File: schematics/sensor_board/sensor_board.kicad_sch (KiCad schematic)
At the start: 6 parts, among them Y1 Crystal

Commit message: I think it is finished.
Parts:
- added C4, C5, C6: 100n, Capacitor_SMD:C_0603_1608Metric_Pad1.08x0.95mm_HandSolder, symbol Device:C
- added J1: Conn_01x06_Pin, Connector_PinHeader_1.27mm:PinHeader_1x06_P1.27mm_Vertical, symbol Connector:Conn_01x06_Pin
- added J2: Conn_01x05_Pin, Connector_PinHeader_1.27mm:PinHeader_1x05_P1.27mm_Vertical, symbol Connector:Conn_01x05_Pin
- added R2, R3, R4, R5, R6, R7, R8, R9: 10k, Resistor_SMD:R_0603_1608Metric_Pad0.98x0.95mm_HandSolder, symbol Device:R
- C1, C2, C3: footprint (none) -> Capacitor_SMD:C_0603_1608Metric_Pad1.08x0.95mm_HandSolder
- R1: value R -> 10k; footprint (none) -> Resistor_SMD:R_0603_1608Metric_Pad0.98x0.95mm_HandSolder
- U1: footprint (none) -> Package_LGA:LGA-28_5.2x3.8mm_P0.5mm
- Y1: footprint (none) -> Crystal:Crystal_HC52-8mm_Vertical
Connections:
- net GND: now also U1.5 (PS1), U1.6 (PS0/WAKE), C4.2, C5.2, C6.2, J1.2 (Pin_2), J2.2 (Pin_2), R3.2
- net VDD: now also C5.1, C6.1, J1.1 (Pin_1), J2.1 (Pin_1), R2.1, R4.1, R5.1, R6.1, R7.1, R8.1, R9.1
- net intn: now reaches U1.14 (H_INTN)
- net intn: now also J1.5 (Pin_5)
- net at U1.15 (ENV_SCL): now also R5.2
- net at U1.16 (ENV_SDA): now also R4.2
- net i2c_addr_sel: now reaches U1.17 (SA0/H_MOSI)
- net i2c_addr_sel: now also R2.2, R3.1
- net at U1.18 (H_CSN): now also R7.2
- net scl: now reaches U1.19 (H_SCL/SCK/RX)
- net scl: now also J1.4 (Pin_4), J2.4 (Pin_4), R8.2
- net sda: now reaches U1.20 (H_SDA/H_MISO/TX)
- net sda: now also J1.3 (Pin_3), J2.3 (Pin_3), R9.2
- net at U1.4 (BOOTN): now also R6.2
- net at U1.9 (CAP): now also C4.1
- new net intn_next: J1.6 (Pin_6), J2.5 (Pin_5)
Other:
- note added: "Add one of these two for I2C address selection."
- note added: "Sampled on reset. If low, enters bootloader mode."
- note added: "This might be not needed. In ref. design it is left not connected."

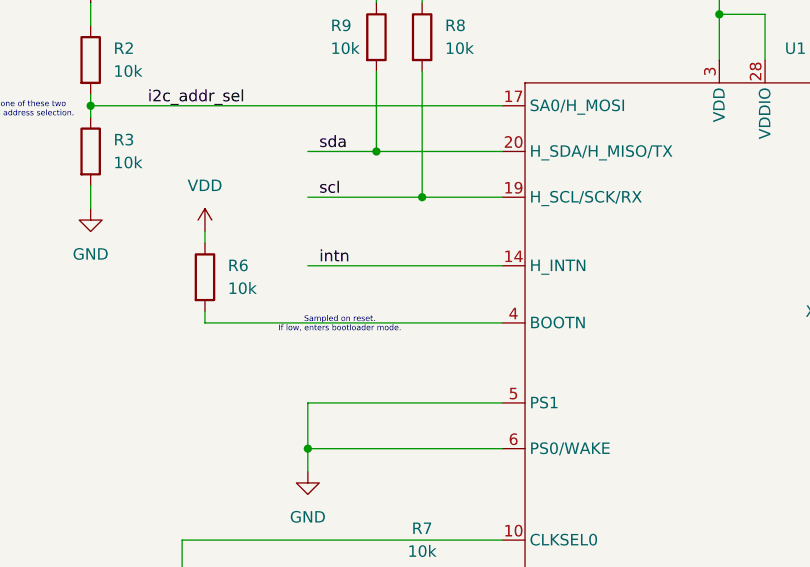
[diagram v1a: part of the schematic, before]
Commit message: Added resistor to the interrupt signal.
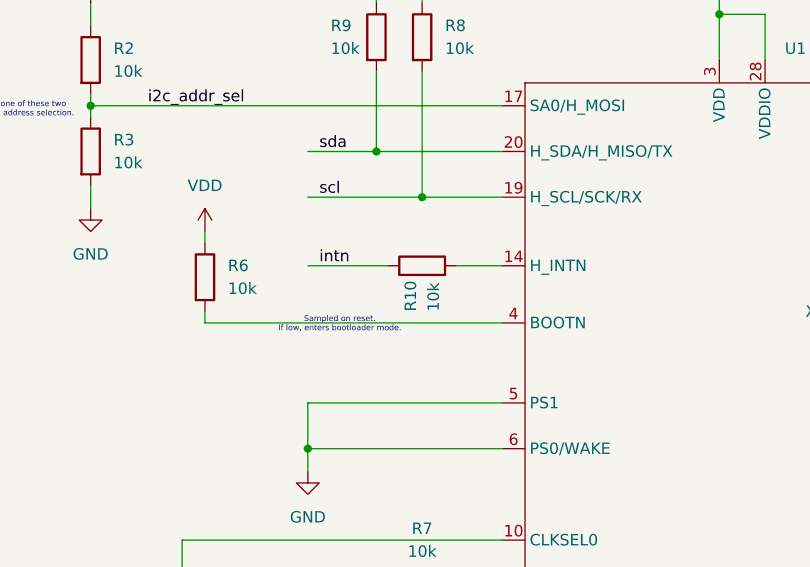
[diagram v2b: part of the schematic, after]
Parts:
- added R10: 10k, Resistor_SMD:R_0603_1608Metric_Pad0.98x0.95mm_HandSolder, symbol Device:R
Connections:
- net intn: now also R10.1; no longer U1.14 (H_INTN)
- new net: R10.2, U1.14 (H_INTN)
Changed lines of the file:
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@@
+	(wire
+		(pts
+			(xy 193.04 105.41) (xy 198.12 105.41)
+		)
+		(stroke
+			(width 0)
+			(type default)
+		)
+	)
 	(wire
 		(pts
@@
 	(wire
 		(pts
-			(xy 176.53 105.41) (xy 198.12 105.41)
-		)
-		(stroke
-			(width 0)
-			(type default)
-		)
-	)
-	(wire
-		(pts
 			(xy 251.46 53.34) (xy 251.46 54.61)
 		)
@@
 		(pts
 			(xy 270.51 148.59) (xy 270.51 153.67)
+		)
+		(stroke
+			(width 0)
+			(type default)
+		)
+	)
+	(wire
+		(pts
+			(xy 176.53 105.41) (xy 185.42 105.41)
 		)
 		(stroke
@@
 					(unit 1)
 				)
+			)
+		)
+	)
+	(symbol
+		(lib_id "Device:R")
+		(at 189.23 105.41 90)
+		(unit 1)
+		(exclude_from_sim no)
+		(in_bom yes)
+		(on_board yes)
+		(dnp no)
+		(property "Reference" "R10"
+			(at 187.96 110.49 0)
+			(effects
+				(font
+					(size 1.27 1.27)
+				)
+				(justify left)
+			)
+		)
+		(property "Value" "10k"
+			(at 190.5 110.49 0)
+			(effects
+				(font
+					(size 1.27 1.27)
+				)
+				(justify left)
+			)
+		)
+		(property "Footprint" "Resistor_SMD:R_0603_1608Metric_Pad0.98x0.95mm_HandSolder"
+			(at 189.23 107.188 90)
+			(effects
+				(font
+					(size 1.27 1.27)
+				)
+				(hide yes)
+			)
+		)
+		(property "Datasheet" "~"
+			(at 189.23 105.41 0)
+			(effects
+				(font
+					(size 1.27 1.27)
+				)
+				(hide yes)
+			)
+		)
+		(property "Description" "Resistor"
+			(at 189.23 105.41 0)
+			(effects
+				(font
+					(size 1.27 1.27)
+				)
+				(hide yes)
+			)
+		)
+		(pin "2"
+		)
+		(pin "1"
+		)
+		(instances
+			(project "sensor_board"
+				(path "/0f022720-add9-458b-9410-e96307841923"
+					(reference "R10")
+					(unit 1)
+				)

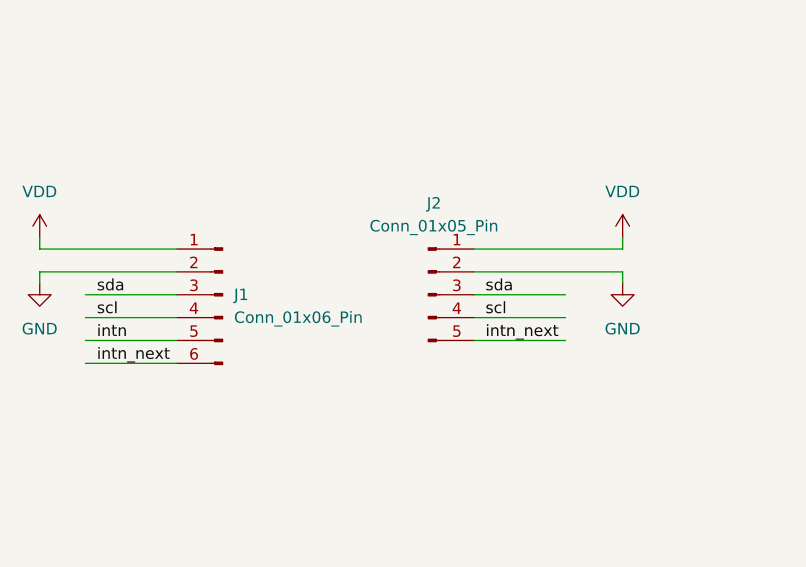
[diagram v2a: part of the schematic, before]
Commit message: Selarated INT, SCL and SDA lines with GND and VDD so that crosstalk is reduced
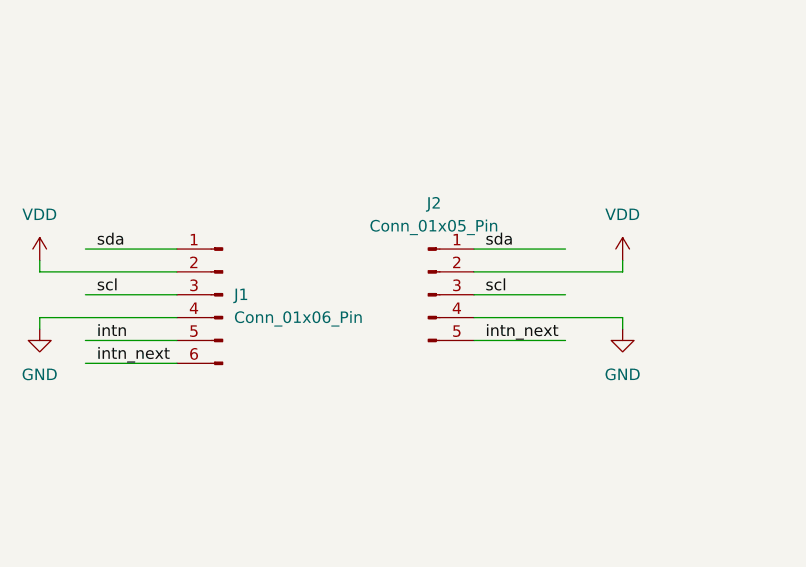
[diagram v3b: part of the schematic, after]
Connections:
- net GND: now also J1.4 (Pin_4), J2.4 (Pin_4); no longer J1.2 (Pin_2), J2.2 (Pin_2)
- net VDD: now also J1.2 (Pin_2), J2.2 (Pin_2); no longer J1.1 (Pin_1), J2.1 (Pin_1)
- net scl: now also J1.3 (Pin_3), J2.3 (Pin_3); no longer J1.4 (Pin_4), J2.4 (Pin_4)
- net sda: now also J1.1 (Pin_1), J2.1 (Pin_1); no longer J1.3 (Pin_3), J2.3 (Pin_3)
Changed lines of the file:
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@@
 	(wire
 		(pts
-			(xy 43.18 100.33) (xy 43.18 101.6)
+			(xy 43.18 102.87) (xy 43.18 104.14)
 		)
 		(stroke
@@
 	(wire
 		(pts
-			(xy 91.44 104.14) (xy 107.95 104.14)
+			(xy 91.44 109.22) (xy 107.95 109.22)
 		)
 		(stroke
@@
 	(wire
 		(pts
-			(xy 48.26 109.22) (xy 58.42 109.22)
+			(xy 48.26 106.68) (xy 58.42 106.68)
 		)
 		(stroke
@@
 	(wire
 		(pts
-			(xy 107.95 100.33) (xy 107.95 101.6)
+			(xy 107.95 102.87) (xy 107.95 104.14)
 		)
 		(stroke
@@
 	(wire
 		(pts
-			(xy 91.44 101.6) (xy 107.95 101.6)
+			(xy 91.44 104.14) (xy 107.95 104.14)
 		)
 		(stroke
@@
 	(wire
 		(pts
-			(xy 43.18 101.6) (xy 58.42 101.6)
+			(xy 43.18 104.14) (xy 58.42 104.14)
 		)
 		(stroke
@@
 	(wire
 		(pts
-			(xy 43.18 104.14) (xy 43.18 105.41)
+			(xy 43.18 109.22) (xy 43.18 110.49)
 		)
 		(stroke
@@
 	(wire
 		(pts
-			(xy 43.18 104.14) (xy 58.42 104.14)
+			(xy 43.18 109.22) (xy 58.42 109.22)
 		)
 		(stroke
@@
 	(wire
 		(pts
-			(xy 107.95 104.14) (xy 107.95 105.41)
+			(xy 107.95 109.22) (xy 107.95 110.49)
 		)
 		(stroke
@@
 	(wire
 		(pts
-			(xy 91.44 106.68) (xy 101.6 106.68)
+			(xy 91.44 101.6) (xy 101.6 101.6)
 		)
 		(stroke
@@
 	(wire
 		(pts
-			(xy 91.44 109.22) (xy 101.6 109.22)
+			(xy 91.44 106.68) (xy 101.6 106.68)
 		)
 		(stroke
@@
 	(wire
 		(pts
-			(xy 48.26 106.68) (xy 58.42 106.68)
+			(xy 48.26 101.6) (xy 58.42 101.6)
 		)
 		(stroke
@@
 	)
 	(label "sda"
-		(at 92.71 106.68 0)
+		(at 92.71 101.6 0)
 		(fields_autoplaced yes)
 		(effects
@@
 	)
 	(label "scl"
-		(at 92.71 109.22 0)
+		(at 92.71 106.68 0)
 		(fields_autoplaced yes)
 		(effects
@@
 	)
 	(label "scl"
-		(at 49.53 109.22 0)
+		(at 49.53 106.68 0)
 		(fields_autoplaced yes)
 		(effects
@@
 	)
 	(label "sda"
-		(at 49.53 106.68 0)
+		(at 49.53 101.6 0)
 		(fields_autoplaced yes)
 		(effects
@@
 	(symbol
 		(lib_id "power:VDD")
-		(at 43.18 100.33 0)
+		(at 43.18 102.87 0)
 		(unit 1)
 		(exclude_from_sim no)
@@
 		(fields_autoplaced yes)
 		(property "Reference" "#PWR019"
-			(at 43.18 104.14 0)
+			(at 43.18 106.68 0)
 			(effects
 				(font
@@
 		)
 		(property "Value" "VDD"
-			(at 43.18 95.25 0)
+			(at 43.18 97.79 0)
 			(effects
 				(font
@@
 		)
 		(property "Footprint" ""
-			(at 43.18 100.33 0)
+			(at 43.18 102.87 0)
 			(effects
 				(font
@@
 		)
 		(property "Datasheet" ""
-			(at 43.18 100.33 0)
+			(at 43.18 102.87 0)
 			(effects
 				(font
@@
 		)
 		(property "Description" "Power symbol creates a global label with name \"VDD\""
-			(at 43.18 100.33 0)
+			(at 43.18 102.87 0)
 			(effects
 				(font
@@
 	(symbol
 		(lib_id "power:GND")
-		(at 107.95 105.41 0)
+		(at 107.95 110.49 0)
 		(unit 1)
 		(exclude_from_sim no)
@@
 		(fields_autoplaced yes)
 		(property "Reference" "#PWR022"
-			(at 107.95 111.76 0)
+			(at 107.95 116.84 0)
 			(effects
 				(font
@@
 		)
 		(property "Value" "GND"
-			(at 107.95 110.49 0)
+			(at 107.95 115.57 0)
 			(effects
 				(font
@@
 		)
 		(property "Footprint" ""
-			(at 107.95 105.41 0)
+			(at 107.95 110.49 0)
 			(effects
 				(font
@@
 		)
 		(property "Datasheet" ""
-			(at 107.95 105.41 0)
+			(at 107.95 110.49 0)
 			(effects
 				(font
@@
 		)
 		(property "Description" "Power symbol creates a global label with name \"GND\" , ground"
-			(at 107.95 105.41 0)
+			(at 107.95 110.49 0)
 			(effects
 				(font
@@
 	(symbol
 		(lib_id "power:VDD")
-		(at 107.95 100.33 0)
+		(at 107.95 102.87 0)
 		(unit 1)
 		(exclude_from_sim no)
@@
 		(fields_autoplaced yes)
 		(property "Reference" "#PWR021"
-			(at 107.95 104.14 0)
+			(at 107.95 106.68 0)
 			(effects
 				(font
@@
 		)
 		(property "Value" "VDD"
-			(at 107.95 95.25 0)
+			(at 107.95 97.79 0)
 			(effects
 				(font
@@
 		)
 		(property "Footprint" ""
-			(at 107.95 100.33 0)
+			(at 107.95 102.87 0)
 			(effects
 				(font
@@
 		)
 		(property "Datasheet" ""
-			(at 107.95 100.33 0)
+			(at 107.95 102.87 0)
 			(effects
 				(font
@@
 		)
 		(property "Description" "Power symbol creates a global label with name \"VDD\""
-			(at 107.95 100.33 0)
+			(at 107.95 102.87 0)
 			(effects
 				(font
@@
 	(symbol
 		(lib_id "power:GND")
-		(at 43.18 105.41 0)
+		(at 43.18 110.49 0)
 		(unit 1)
 		(exclude_from_sim no)
@@
 		(fields_autoplaced yes)
 		(property "Reference" "#PWR020"
-			(at 43.18 111.76 0)
+			(at 43.18 116.84 0)
 			(effects
 				(font
@@
 		)
 		(property "Value" "GND"
-			(at 43.18 110.49 0)
+			(at 43.18 115.57 0)
 			(effects
 				(font
@@
 		)
 		(property "Footprint" ""
-			(at 43.18 105.41 0)
+			(at 43.18 110.49 0)
 			(effects
 				(font
@@
 		)
 		(property "Datasheet" ""
-			(at 43.18 105.41 0)
+			(at 43.18 110.49 0)
 			(effects
 				(font
@@
 		)
 		(property "Description" "Power symbol creates a global label with name \"GND\" , ground"
-			(at 43.18 105.41 0)
+			(at 43.18 110.49 0)
 			(effects
 				(font
